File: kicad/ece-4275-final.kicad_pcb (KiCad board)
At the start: 2 copper layers, 96.5 x 63.5 mm, 10 parts, among them U1 ESP32-S3, U2 LMR36015ARNXR, U3 AMS1117-3.3

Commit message: finish motor driver module
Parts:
- removed U1: ESP32-S3, Package_DFN_QFN:QFN-56-1EP_7x7mm_P0.4mm_EP4x4mm
- added C13: 1uF, Capacitor_SMD:C_0402_1005Metric, F.Cu at (169.9, 97.5)
- added C14: 4.7uF, Capacitor_SMD:C_0402_1005Metric, F.Cu at (169.9, 99.5)
- added CBOOT2: 0.1uF, Capacitor_SMD:C_0402_1005Metric, F.Cu at (169.9, 101.4)
- added CFF2: 20uF, Capacitor_SMD:C_0402_1005Metric, F.Cu at (169.9, 103.4)
- added CHF3: 220nF, Capacitor_SMD:C_0402_1005Metric, F.Cu at (169.9, 105.4)
- added CHF4: 220nF, Capacitor_SMD:C_0402_1005Metric, F.Cu at (169.9, 107.3)
- added Cin2: 4.7uF, Capacitor_SMD:C_0402_1005Metric, F.Cu at (169.9, 109.3)
- added U2: ESP32-C6-MINI-1, RF_Module:ESP32-C6-MINI-1, F.Cu at (108.0, 54.5)
- added U3: AMS1117-3.3, Package_TO_SOT_SMD:SOT-223-3_TabPin2, F.Cu at (176.3, 100.7)
- added U4: ~, PCM_Espressif:ESP32-P4, F.Cu at (141.2, 79.0)
- added U5: TMC5160A-TA, Package_QFP:TQFP-48-1EP_7x7mm_P0.5mm_EP5x5mm_ThermalVias, F.Cu at (188.9, 102.2)
- added U6: LMR36015ARNXR, IMPORTS:LMR36015, F.Cu at (173.1, 107.0)
- moved CHF2 54.6 mm to (156.4, 107.3), turned to 90 degrees
- moved CHF1 53.5 mm to (154.4, 107.3), turned to 90 degrees
- moved Cin1 52.7 mm to (152.4, 107.3), turned to 90 degrees
- moved U2 52.3 mm to (148.7, 107.5), turned to 180 degrees
- moved C4 46.1 mm to (142.1, 103.7), turned to 180 degrees
- moved C6 42.3 mm to (142.1, 101.7), turned to 180 degrees
- moved CBOOT1 38.5 mm to (142.1, 99.8), turned to 180 degrees
- moved U3 38.3 mm to (148.5, 100.5), turned to 180 degrees
- moved CFF1 34.7 mm to (142.1, 97.8), turned to 180 degrees
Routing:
- net Net-(U2-GND-Pad1): vias 0 -> 9

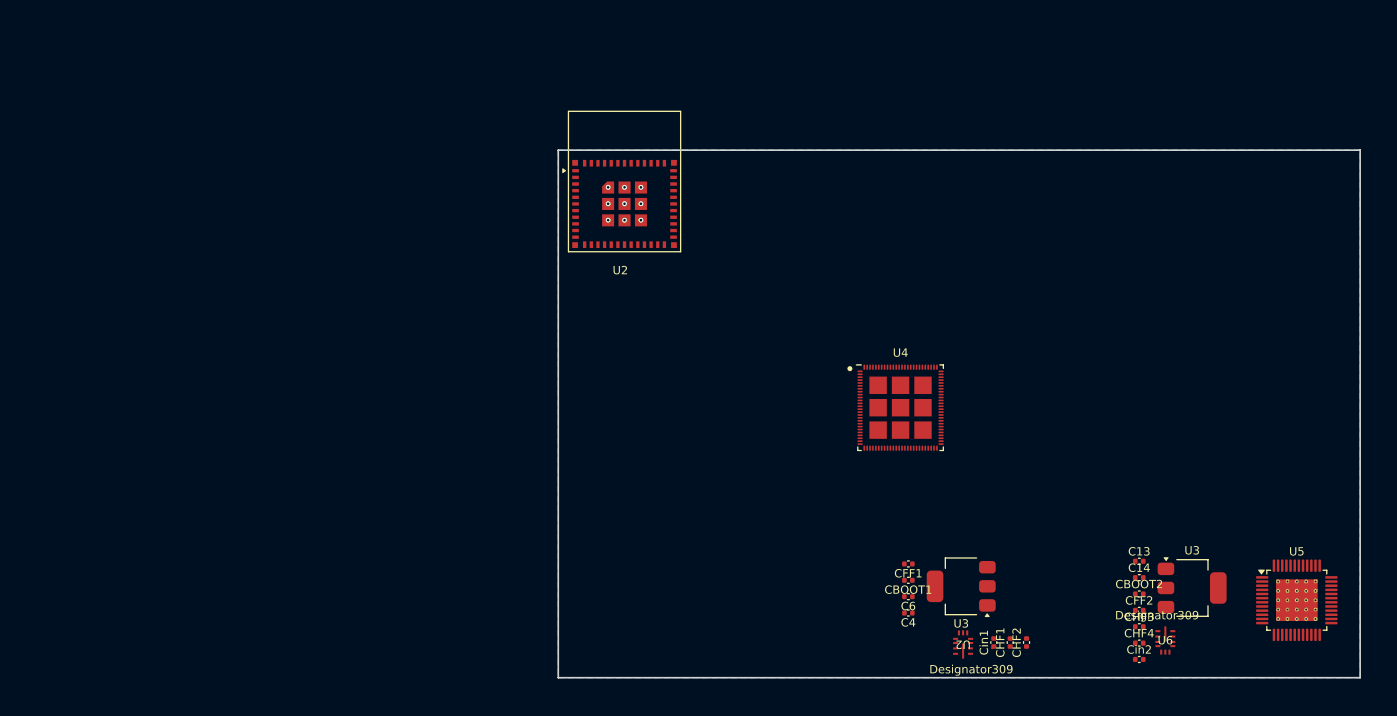
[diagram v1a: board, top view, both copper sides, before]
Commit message: add usb connector
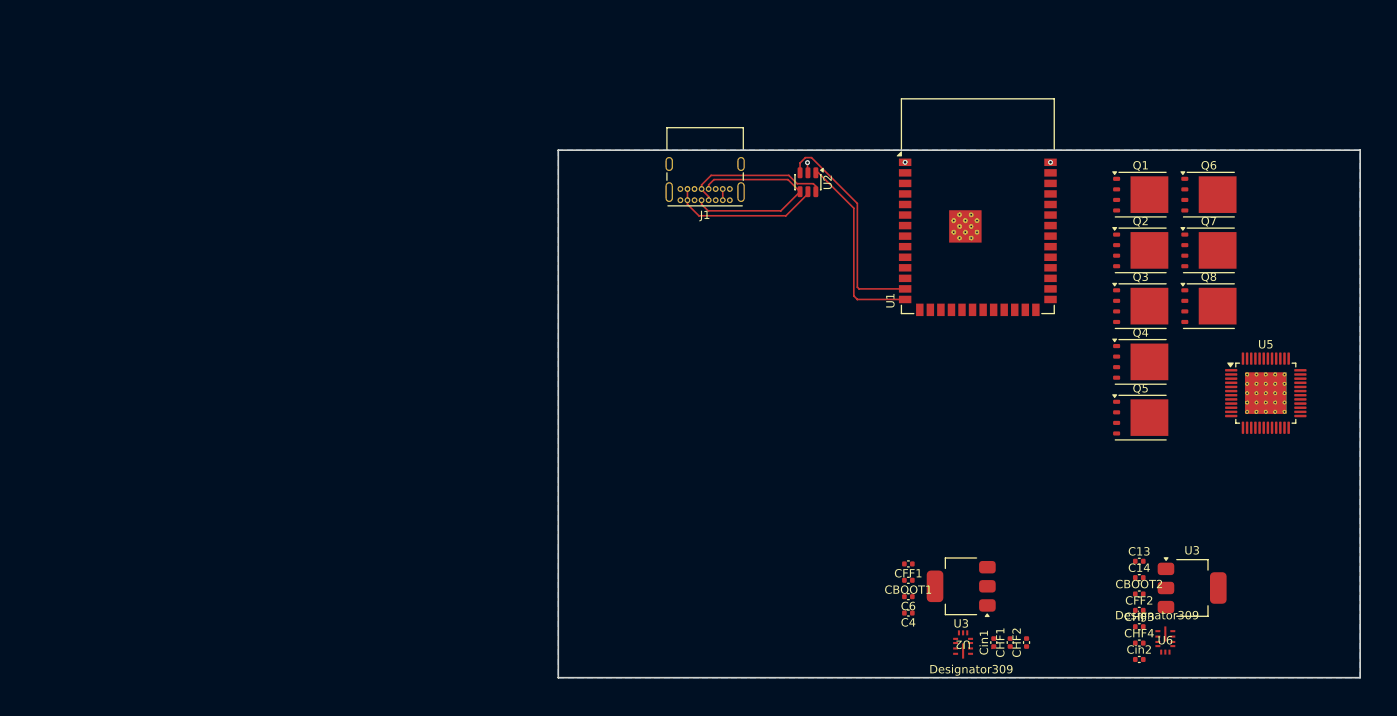
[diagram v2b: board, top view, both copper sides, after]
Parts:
- removed U4: ~, PCM_Espressif:ESP32-P4
- added J1: USB_C_Receptacle_USB2.0_14P, Connector_USB:USB_C_Receptacle_GCT_USB4085, F.Cu at (120.7, 54.0)
- added Q1: BSC440N10NS3G, Package_TO_SOT_SMD:TDSON-8-1, F.Cu at (170.1, 53.4)
- added Q2: BSC440N10NS3G, Package_TO_SOT_SMD:TDSON-8-1, F.Cu at (170.1, 60.1)
- added Q3: BSC440N10NS3G, Package_TO_SOT_SMD:TDSON-8-1, F.Cu at (170.1, 66.8)
- added Q4: BSC440N10NS3G, Package_TO_SOT_SMD:TDSON-8-1, F.Cu at (170.1, 73.5)
- added Q5: BSC440N10NS3G, Package_TO_SOT_SMD:TDSON-8-1, F.Cu at (170.1, 80.2)
- added Q6: BSC440N10NS3G, Package_TO_SOT_SMD:TDSON-8-1, F.Cu at (178.3, 53.4)
- added Q7: BSC440N10NS3G, Package_TO_SOT_SMD:TDSON-8-1, F.Cu at (178.3, 60.1)
- added Q8: BSC440N10NS3G, Package_TO_SOT_SMD:TDSON-8-1, F.Cu at (178.3, 66.8)
- added U1: ESP32-S3-WROOM-1, RF_Module:ESP32-S3-WROOM-1, F.Cu at (150.5, 54.7)
- U2: value ESP32-C6-MINI-1 -> USBLC6-2SC6; footprint RF_Module:ESP32-C6-MINI-1 -> Package_TO_SOT_SMD:SOT-23-6
- moved U5 25.2 mm to (185.2, 77.2)
- moved U2 22.2 mm to (130.1, 51.9), turned to -90 degrees
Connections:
- U2 pad 1: Net-(U2-GND-Pad1) -> Net-(U1-USB_D+)
- U2 pad 2: Net-(U2-GND-Pad1) -> GND
- U2 pad 3: unconnected-(U2-3V3-Pad3) -> Net-(U1-USB_D-)
- U2 pad 4: unconnected-(U2-NC-Pad4) -> Net-(J1-D--PadA7)
- U2 pad 5: unconnected-(U2-IO2-Pad5) -> +5V
- U2 pad 6: unconnected-(U2-IO3-Pad6) -> Net-(J1-D+-PadA6)
- U5 pad 1: unconnected-(U5-HB1-Pad1) -> Net-(U5-HB1)
- U5 pad 10: unconnected-(U5-SRBL-Pad10) -> Net-(U5-SRBL)
- U5 pad 11: unconnected-(U5-TST_MODE-Pad11) -> /Stepper Motor Module/TST_MODE
- U5 pad 17: unconnected-(U5-REFL/STEP-Pad17) -> /Stepper Motor Module/REFL_STEP
- U5 pad 18: unconnected-(U5-REFR/DIR-Pad18) -> /Stepper Motor Module/REFL_DIR
- U5 pad 2: unconnected-(U5-CB1-Pad2) -> Net-(U5-CB1)
- U5 pad 21: unconnected-(U5-SD_MODE-Pad21) -> /Stepper Motor Module/SD_MODE
- U5 pad 22: unconnected-(U5-SPI_MODE-Pad22) -> /Stepper Motor Module/SPI_MODE
- U5 pad 23: unconnected-(U5-ENCB/DCEN/CFG4-Pad23) -> /Stepper Motor Module/ENC_B_DCEN
- U5 pad 24: unconnected-(U5-ENCA/DCIN/CFG5-Pad24) -> /Stepper Motor Module/ENC_A_DCIN
- U5 pad 25: unconnected-(U5-ENCN/DCO/CFG6-Pad25) -> /Stepper Motor Module/ENC_N_DCO
- U5 pad 26: unconnected-(U5-SWN/DIAG0-Pad26) -> /Stepper Motor Module/DIAG0_SWN
- U5 pad 27: unconnected-(U5-SWP/DIAG1-Pad27) -> /Stepper Motor Module/DIAG1_SWP
- U5 pad 31: unconnected-(U5-CPO-Pad31) -> Net-(U5-CPO)
- U5 pad 32: unconnected-(U5-CPI-Pad32) -> Net-(U5-CPI)
- U5 pad 35: unconnected-(U5-CA2-Pad35) -> Net-(U5-CA2)
- U5 pad 36: unconnected-(U5-HA2-Pad36) -> Net-(U5-HA2)
- U5 pad 37: unconnected-(U5-BMA2-Pad37) -> /Stepper Motor Module/A2
- U5 pad 38: unconnected-(U5-LA2-Pad38) -> Net-(U5-LA2)
- U5 pad 39: unconnected-(U5-LA1-Pad39) -> Net-(U5-LA1)
- U5 pad 40: unconnected-(U5-BMA1-Pad40) -> /Stepper Motor Module/A1
- U5 pad 41: unconnected-(U5-HA1-Pad41) -> Net-(U5-HA1)
- U5 pad 42: unconnected-(U5-CA1-Pad42) -> Net-(U5-CA1)
- U5 pad 43: unconnected-(U5-CB2-Pad43) -> Net-(U5-CB2)
- U5 pad 44: unconnected-(U5-HB2-Pad44) -> Net-(U5-HB2)
- U5 pad 45: unconnected-(U5-BMB2-Pad45) -> /Stepper Motor Module/B2
- U5 pad 46: unconnected-(U5-LB2-Pad46) -> Net-(Q4-D)
- U5 pad 47: unconnected-(U5-LB1-Pad47) -> Net-(U5-LB1)
- U5 pad 48: unconnected-(U5-BMB1-Pad48) -> /Stepper Motor Module/B1
- U5 pad 7: unconnected-(U5-SRAL-Pad7) -> Net-(U5-SRAL)
- U5 pad 8: unconnected-(U5-SRAH-Pad8) -> Net-(U5-SRAH)
- U5 pad 9: unconnected-(U5-SRBH-Pad9) -> Net-(U5-SRBH)
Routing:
- net Net-(U1-USB_D-): track 0.00 -> 26.5 mm
- net Net-(J1-D--PadA7): track 0.00 -> 26.0 mm
- net Net-(U1-USB_D+): track 0.00 -> 23.5 mm
- net +5V: track 0.00 -> 20.0 mm
- net Net-(J1-D+-PadA6): track 0.00 -> 17.7 mm
- net GND: track 0.00 -> 0.86 mm, vias 0 -> 3
- net Net-(U2-GND-Pad1): vias 9 -> 0

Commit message: edit a lot of stuff
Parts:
- removed CBOOT1: 0.1uF, Capacitor_SMD:C_0402_1005Metric
- removed CFF1: 20uF, Capacitor_SMD:C_0402_1005Metric
- removed CHF1, CHF2: 220nF, Capacitor_SMD:C_0402_1005Metric
- removed Cin1: 4.7uF, Capacitor_SMD:C_0402_1005Metric
- removed the U2 at (148.7, 107.5)
- removed the U3 at (148.5, 100.5)
- removed the U3 at (176.3, 100.7)
- added BOOT1: SW_Omron_B3FS, Button_Switch_SMD:SW_Push_1P1T-SH_NO_CK_KMR2xxG, F.Cu at (66.7, 57.4)
- added C1: CB, Capacitor_SMD:C_0402_1005Metric, F.Cu at (180.7, 95.0)
- added C10: 0.1uF, Capacitor_SMD:C_0402_1005Metric, F.Cu at (90.1, 77.4)
- added C15: 470nF, Capacitor_SMD:C_0402_1005Metric, F.Cu at (183.6, 100.9)
- added C16: 100nF, Capacitor_SMD:C_0402_1005Metric, F.Cu at (183.6, 102.9)
- added C17: 100nF, Capacitor_SMD:C_0402_1005Metric, F.Cu at (186.5, 95.0)
- added C18: 100nF, Capacitor_SMD:C_0402_1005Metric, F.Cu at (186.5, 97.0)
- added C19: 470nF, Capacitor_SMD:C_0402_1005Metric, F.Cu at (186.5, 99.0)
- added C2: 100nF, Capacitor_SMD:C_0402_1005Metric, F.Cu at (180.7, 97.0)
- added C20: 470nF, Capacitor_SMD:C_0402_1005Metric, F.Cu at (186.5, 100.9)
- added C3: CB, Capacitor_SMD:C_0402_1005Metric, F.Cu at (180.7, 99.0)
- added C5: CB, Capacitor_SMD:C_0402_1005Metric, F.Cu at (180.7, 102.9)
- added C7: CB, Capacitor_SMD:C_0402_1005Metric, F.Cu at (183.6, 97.0)
- added C8: 22n, 100V, Capacitor_SMD:C_0402_1005Metric, F.Cu at (183.6, 99.0)
- added C9: 10uF, Capacitor_SMD:C_0402_1005Metric, F.Cu at (90.1, 75.4)
- added C_E1: C_Polarized, Capacitor_SMD:CP_Elec_3x5.3, F.Cu at (128.5, 104.0)
- added EN1: SW_Omron_B3FS, Button_Switch_SMD:SW_Push_1P1T-SH_NO_CK_KMR2xxG, F.Cu at (66.7, 72.9)
- added J2: Screw_Terminal_01x02, TerminalBlock:TerminalBlock_MaiXu_MX126-5.0-02P_1x02_P5.00mm, F.Cu at (134.0, 109.5)
- added J3: Conn_01x08, Connector_PinHeader_2.54mm:PinHeader_1x08_P2.54mm_Vertical, F.Cu at (102.0, 90.9)
- added J4: Conn_01x08, Connector_PinHeader_2.54mm:PinHeader_1x08_P2.54mm_Vertical, F.Cu at (78.0, 35.3)
- added J5: Conn_01x02, Connector_PinHeader_2.54mm:PinHeader_1x02_P2.54mm_Vertical, F.Cu at (194.5, 107.0)
- added L2: 15uH, Inductor_SMD:L_6.3x6.3_H3, F.Cu at (120.2, 94.0)
- added Q9: AO3400A, Package_TO_SOT_SMD:SOT-23, F.Cu at (181.9, 106.0)
- added R1: 2R2, Resistor_SMD:R_0402_1005Metric, F.Cu at (172.0, 95.0)
- added R10: RS, Resistor_SMD:R_0402_1005Metric, F.Cu at (174.9, 101.0)
- added R11: RG, Resistor_SMD:R_0402_1005Metric, F.Cu at (174.9, 103.0)
- added R12: RG, Resistor_SMD:R_0402_1005Metric, F.Cu at (174.9, 105.0)
- added R13: 47, Resistor_SMD:R_0402_1005Metric, F.Cu at (177.8, 95.0)
- added R14: 47, Resistor_SMD:R_0402_1005Metric, F.Cu at (177.8, 97.0)
- added R15: RS, Resistor_SMD:R_0402_1005Metric, F.Cu at (177.8, 99.0)
- added R16: R, Resistor_SMD:R_0402_1005Metric, F.Cu at (82.7, 75.5)
- added R17: R, Resistor_SMD:R_0402_1005Metric, F.Cu at (82.7, 77.4)
- added R18: 5.1k, Resistor_SMD:R_0402_1005Metric, F.Cu at (82.7, 79.4)
- added R19: 5.1k, Resistor_SMD:R_0402_1005Metric, F.Cu at (82.7, 81.4)
- added R2: RG, Resistor_SMD:R_0402_1005Metric, F.Cu at (172.0, 97.0)
- added R3: RG, Resistor_SMD:R_0402_1005Metric, F.Cu at (172.0, 99.0)
- added R4: RG, Resistor_SMD:R_0402_1005Metric, F.Cu at (172.0, 101.0)
- added R5: RG, Resistor_SMD:R_0402_1005Metric, F.Cu at (172.0, 103.0)
- added R6: RG, Resistor_SMD:R_0402_1005Metric, F.Cu at (172.0, 105.0)
- added R7: RG, Resistor_SMD:R_0402_1005Metric, F.Cu at (174.9, 95.0)
- added R8: 47, Resistor_SMD:R_0402_1005Metric, F.Cu at (174.9, 97.0)
- added R9: 47, Resistor_SMD:R_0402_1005Metric, F.Cu at (174.9, 99.0)
- added RFBB2: 10k, Resistor_SMD:R_0402_1005Metric, F.Cu at (73.8, 78.6)
- added RFBT2: 52.3k, Resistor_SMD:R_0402_1005Metric, F.Cu at (73.8, 80.6)
- added U3: AMS1117-3.3, Package_TO_SOT_SMD:SOT-223-3_TabPin2, F.Cu at (147.8, 106.5)
- C4: value 1uF -> 2.2uF
- C6: value 4.7uF -> 2.2uF
- Q1, Q2, Q3, Q4, Q5, Q6, Q7, Q8: value BSC440N10NS3G -> BSZ150N10NS3-G; footprint Package_TO_SOT_SMD:TDSON-8-1 -> Package_SON:VSON-8_3.3x3.3mm_P0.65mm_NexFET
- moved C6 42.0 mm to (183.6, 95.0), turned to 0 degrees
- moved C14 41.7 mm to (128.5, 95.0), turned to 90 degrees
- moved C13 41.5 mm to (128.5, 99.0), turned to 90 degrees
- moved U6 39.2 mm to (134.0, 103.5), turned to -90 degrees
- moved Q6 39.2 mm to (167.4, 91.0), turned to 90 degrees
- moved C4 38.7 mm to (180.7, 100.9), turned to 0 degrees
- moved CBOOT2 38.0 mm to (132.5, 95.0), turned to 90 degrees
- moved CFF2 37.7 mm to (132.5, 99.0), turned to 90 degrees
- moved CHF3 35.6 mm to (136.0, 94.5), turned to 90 degrees
- moved Q1 35.3 mm to (156.8, 86.0), turned to 90 degrees
- moved Q2 33.6 mm to (156.8, 91.0), turned to 90 degrees
- moved CHF4 33.0 mm to (138.9, 96.0), turned to 90 degrees
- moved Cin2 31.9 mm to (140.9, 96.0), turned to 90 degrees
- moved U5 31.1 mm to (164.8, 100.8)
- moved Q7 26.5 mm to (172.7, 86.0), turned to 90 degrees
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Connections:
- C4 pad 1: Net-(U2-VCC) -> GND
- C4 pad 2: GND -> Net-(U5-12VOUT)
- C6 pad 1: Net-(C6-Pad1) -> GND
- C6 pad 2: GND -> Net-(U5-5VOUT)
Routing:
- net GND: track 0.86 -> 156.5 mm, vias 3 -> 14
- net Net-(U1-IO0): track 0.00 -> 129.3 mm
- net Net-(Q8-G): track 0.00 -> 117.5 mm
- net Net-(Q7-G): track 0.00 -> 114.2 mm
- net /Stepper Motor Module/B2: track 0.00 -> 109.9 mm
- net Net-(J1-CC1): track 0.00 -> 92.3 mm, vias 0 -> 1
- net Net-(U6-FB): track 0.00 -> 80.5 mm
- net Net-(C14-Pad1): track 0.00 -> 70.3 mm
- net +48V: track 0.32 -> 52.6 mm
- net unconnected-(U5-EP-Pad49): track 0.00 -> 27.0 mm
- net Net-(U1-USB_D-): track 26.5 -> 47.0 mm
- net +5V: track 20.0 -> 40.2 mm
- net Net-(U1-EN): track 0.00 -> 19.3 mm
- net Net-(J1-D+-PadA6): track 17.7 -> 32.5 mm
- net Net-(Q4-D): track 0.00 -> 14.3 mm
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
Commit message: update pcb routing:
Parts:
- added J6: STEPPER_1_JST_XH, Connector_JST:JST_XH_B4B-XH-A_1x04_P2.50mm_Vertical, F.Cu at (104.1, 61.2)
- Q1, Q2, Q3, Q4, Q5, Q6, Q7, Q8: value BSZ150N10NS3-G -> BSZ150N10LS3-G
- moved J3 92.3 mm to (194.1, 85.2)
- moved C20 84.4 mm to (114.2, 57.3)
- moved C19 83.2 mm to (115.1, 56.2)
- moved C5 81.1 mm to (109.5, 64.1)
- moved C17 78.8 mm to (116.7, 58.3), turned to 90 degrees
- moved C18 78.5 mm to (118.7, 57.3), turned to -90 degrees
- moved C7 78.4 mm to (115.7, 57.7), turned to -90 degrees
- moved R11 76.7 mm to (108.1, 65.3), turned to 180 degrees
- moved C15 76.5 mm to (120.7, 57.3), turned to -90 degrees
- moved C8 76.2 mm to (118.8, 58.9), turned to 180 degrees
- moved C1 75.6 mm to (111.2, 65.4), turned to -90 degrees
- moved R12 75.2 mm to (109.7, 67.6), turned to 180 degrees
- moved C2 74.5 mm to (117.7, 57.3), turned to 90 degrees
- moved C3 74.3 mm to (112.2, 70.1), turned to 90 degrees
- moved C4 70.8 mm to (116.2, 71.9), turned to 90 degrees
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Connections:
- net /Stepper Motor Module/CS renamed /DRV_1_CS
- net /Stepper Motor Module/REFL_DIR renamed /DRV_1_DIR
- net /Stepper Motor Module/REFL_STEP renamed /DRV_1_STEP
- C14 pad 1: Net-(C14-Pad1) -> +5V
- C19 pad 1: unconnected-(C19-Pad1) -> GND
- CFF2 pad 1: Net-(C14-Pad1) -> +5V
- L2 pad 2: Net-(C14-Pad1) -> +5V
- RFBT2 pad 1: Net-(C14-Pad1) -> +5V
- U1 pad 19: unconnected-(U1-IO11-Pad19) -> /DRV_MOSI
- U1 pad 20: unconnected-(U1-IO12-Pad20) -> /DRV_SCK
- U1 pad 21: unconnected-(U1-IO13-Pad21) -> /DRV_MISO
- U1 pad 22: unconnected-(U1-IO14-Pad22) -> /DRV_ENA
- U3 pad 2: Net-(U3-VO) -> +3.3V
- U3 pad 3: Net-(U3-VI) -> +5V
- U5 pad 11: /Stepper Motor Module/TST_MODE -> GND
- U5 pad 12: /Stepper Motor Module/CLK -> GND
- U5 pad 14: /Stepper Motor Module/SPI_SCK -> /DRV_SCK
- U5 pad 15: /Stepper Motor Module/SPI_MOSI -> /DRV_MOSI
- U5 pad 16: /Stepper Motor Module/SPI_MISO -> /DRV_MISO
- U5 pad 21: /Stepper Motor Module/SD_MODE -> +3.3V
- U5 pad 22: /Stepper Motor Module/SPI_MODE -> +3.3V
- U5 pad 23: /Stepper Motor Module/ENC_B_DCEN -> GND
- U5 pad 24: /Stepper Motor Module/ENC_A_DCIN -> GND
- U5 pad 25: /Stepper Motor Module/ENC_N_DCO -> GND
- U5 pad 26: /Stepper Motor Module/DIAG0_SWN -> GND
- U5 pad 27: /Stepper Motor Module/DIAG1_SWP -> GND
- U5 pad 28: /Stepper Motor Module/DRV_ENA -> /DRV_ENA
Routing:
- net Net-(U1-IO0): track 129.3 -> 0.00 mm
- net Net-(Q7-G): track 114.2 -> 0.00 mm
- net GND: track 156.5 -> 42.9 mm
- net Net-(Q8-G): track 117.5 -> 18.3 mm, vias 0 -> 2
- net Net-(J1-CC1): track 92.3 -> 0.00 mm, vias 1 -> 0
- net Net-(U6-FB): track 80.5 -> 0.00 mm
- net Net-(C14-Pad1): track 70.3 -> 0.00 mm
- net +48V: track 52.6 -> 122.8 mm
- net /Stepper Motor Module/B2: track 109.9 -> 44.8 mm, vias 0 -> 2
- net +3.3V: track 11.4 -> 68.6 mm, vias 0 -> 2
- net /Stepper Motor Module/A2: track 4.68 -> 52.0 mm, vias 0 -> 2
- net /DRV_ENA: track 0.00 -> 38.9 mm, vias 0 -> 2
- net /DRV_MISO: track 0.00 -> 30.5 mm
- net /Stepper Motor Module/A1: track 4.56 -> 32.5 mm, vias 0 -> 2
- net /Stepper Motor Module/B1: track 4.42 -> 31.1 mm, vias 0 -> 1
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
